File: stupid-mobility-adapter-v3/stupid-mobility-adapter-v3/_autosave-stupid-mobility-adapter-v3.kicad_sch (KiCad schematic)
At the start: 38 parts, among them J1 BTS7968-0, J10 UART, J2 Act0-FB, J3 BTS7968-1, J4 Act1-FB, J5 ESTOP_INPUT, J6 UART, J7 Relays, J8 I2C, J9 BATT_MON_SELECT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

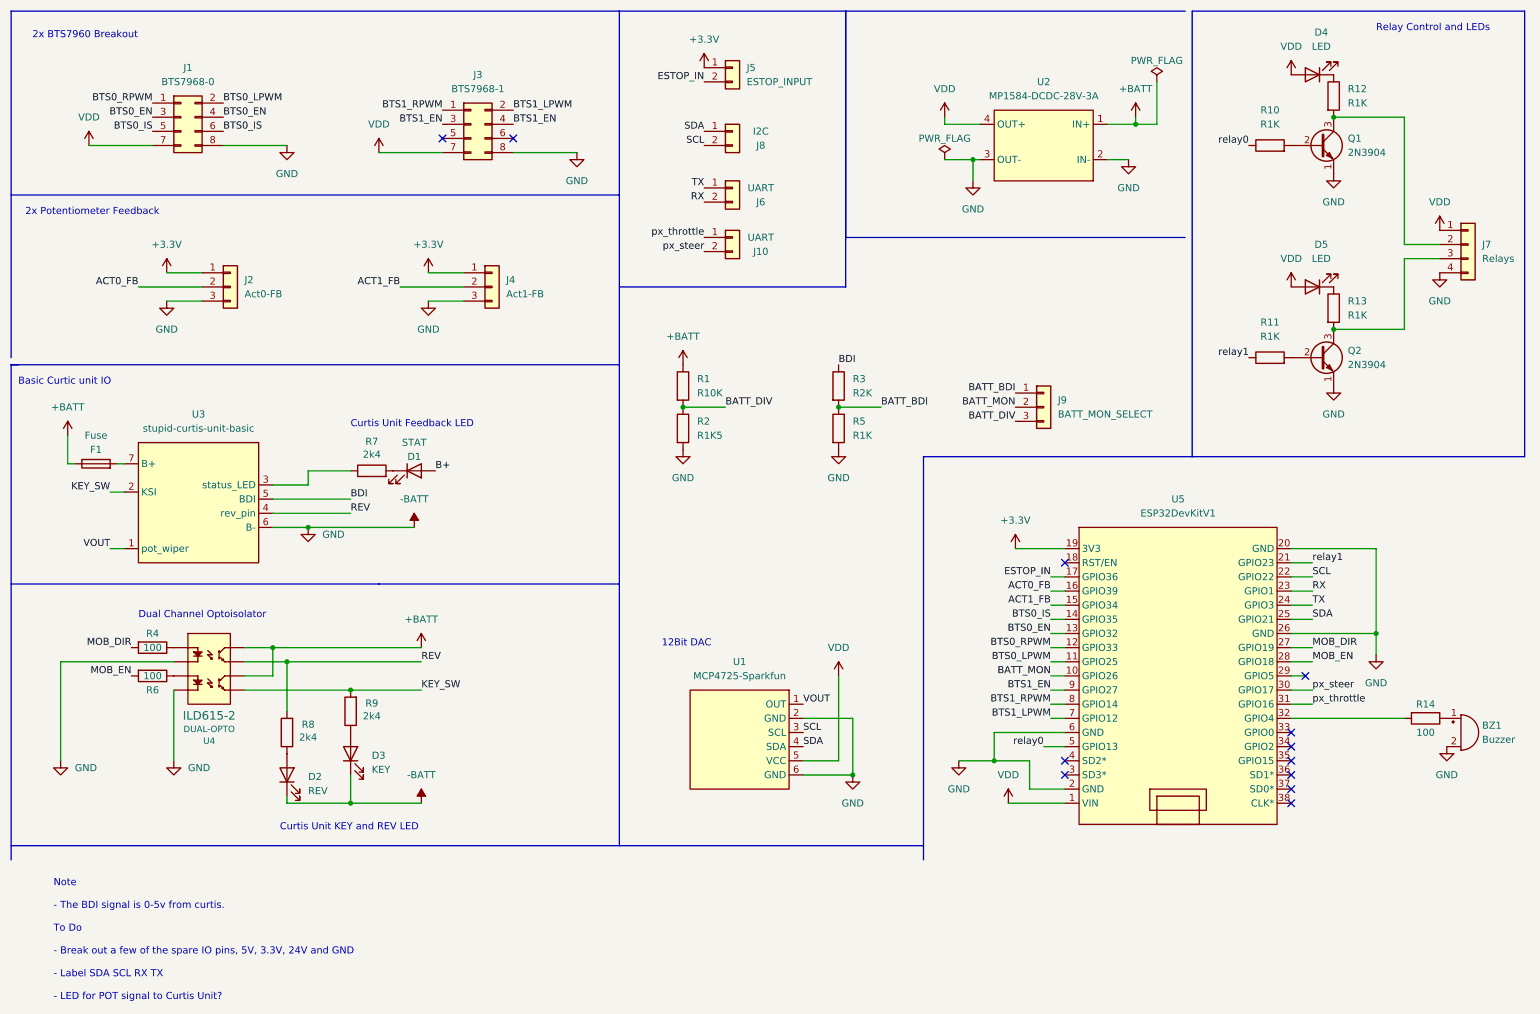
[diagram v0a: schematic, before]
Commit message: Commit before doing first fork for new project
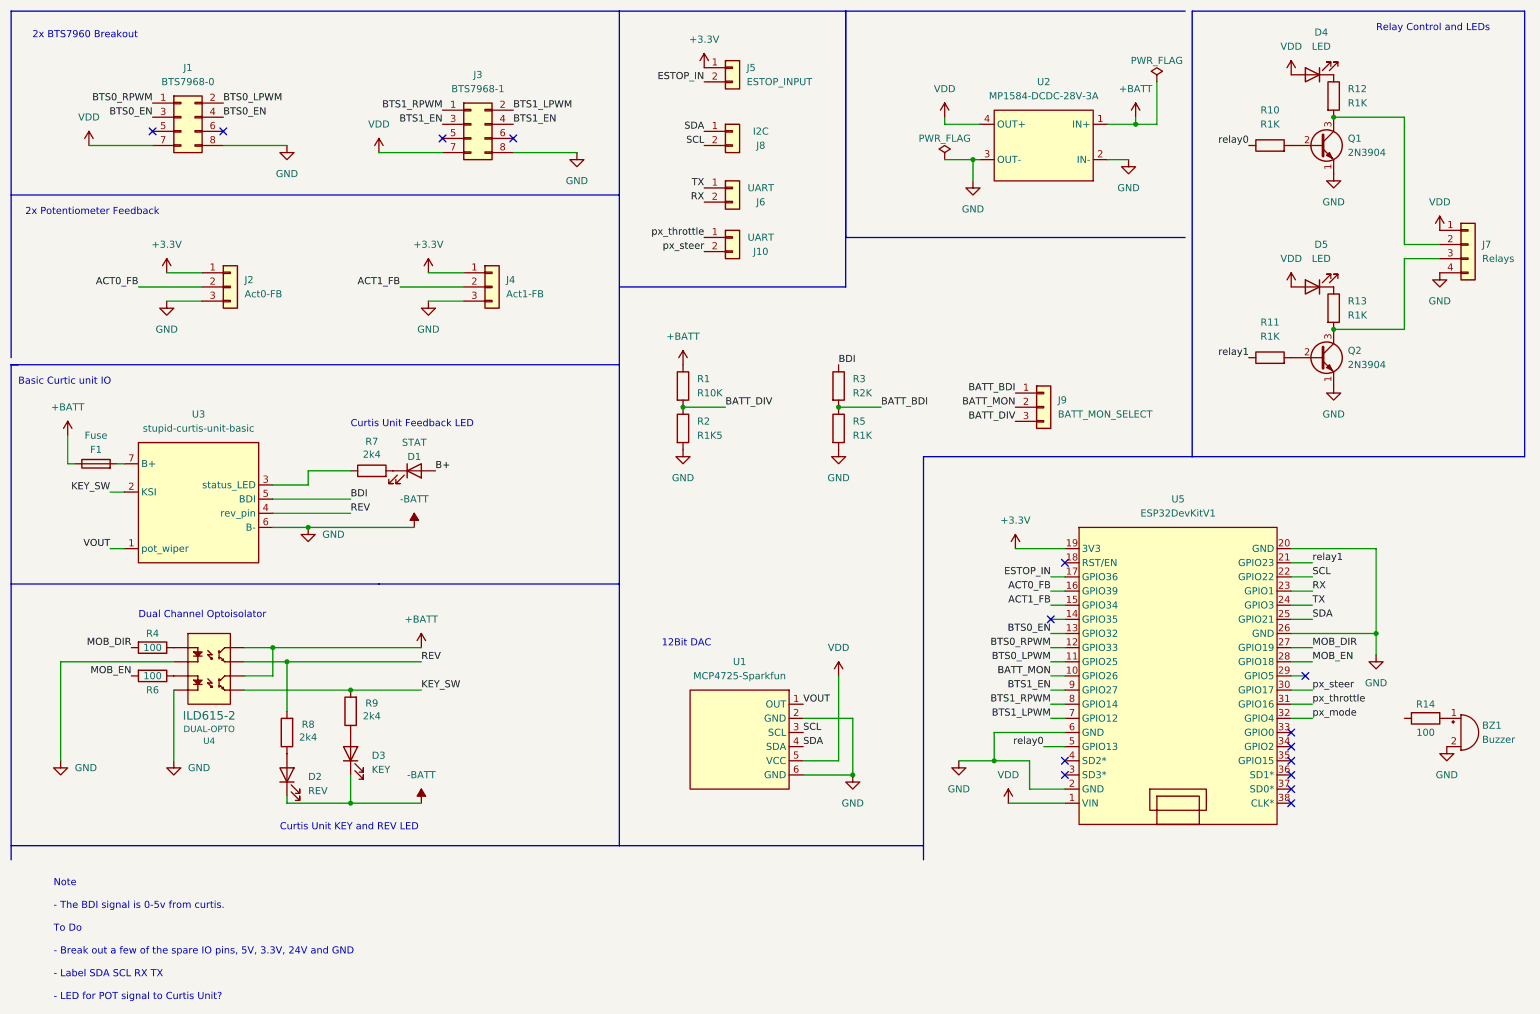
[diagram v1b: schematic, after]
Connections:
- net at R14.2: no longer U5.32 (GPIO4)
- removed net BTS0_IS: J1.5 (Pin_5), J1.6 (Pin_6), U5.14 (GPIO35)
- new net px_mode: U5.32 (GPIO4)
- no-connect marks 12 -> 15
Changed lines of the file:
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@@
   (no_connect (at 242.57 154.94))
   (no_connect (at 242.57 152.4))
+  (no_connect (at 38.1 34.29))
   (no_connect (at 201.93 149.86))
   (no_connect (at 245.11 132.08))
+  (no_connect (at 50.8 34.29))
   (no_connect (at 201.93 147.32))
+  (no_connect (at 199.39 121.92))
   (no_connect (at 102.87 35.56))
   (no_connect (at 90.17 35.56))
@@
     (stroke (width 0) (type default) (color 0 0 0 0))
   )
+  (wire (pts (xy 242.57 139.7) (xy 246.38 139.7))
+    (stroke (width 0) (type default) (color 0 0 0 0))
+  )
   (wire (pts (xy 242.57 114.3) (xy 246.38 114.3))
-    (stroke (width 0) (type default) (color 0 0 0 0))
-  )
-  (wire (pts (xy 262.89 139.7) (xy 242.57 139.7))
     (stroke (width 0) (type default) (color 0 0 0 0))
   )
@@
     (effects (font (size 1.27 1.27)) (justify left bottom))
   )
-  (label "BTS0_IS" (at 38.1 34.29 180)
-    (effects (font (size 1.27 1.27)) (justify right bottom))
-  )
   (label "ESTOP_IN" (at 199.39 114.3 180)
     (effects (font (size 1.27 1.27)) (justify right bottom))
@@
   )
   (label "relay1" (at 246.38 111.76 0)
+    (effects (font (size 1.27 1.27)) (justify left bottom))
+  )
+  (label "px_mode" (at 246.38 139.7 0)
     (effects (font (size 1.27 1.27)) (justify left bottom))
   )
@@
     (effects (font (size 1.2446 1.2446)) (justify left bottom))
   )
-  (label "BTS0_IS" (at 199.39 121.92 180)
-    (effects (font (size 1.27 1.27)) (justify right bottom))
-  )
   (label "BTS0_EN" (at 38.1 31.75 180)
     (effects (font (size 1.27 1.27)) (justify right bottom))
   )
-  (label "BTS0_IS" (at 50.8 34.29 0)
-    (effects (font (size 1.27 1.27)) (justify left bottom))
-  )
   (label "BTS1_EN" (at 199.39 134.62 180)
